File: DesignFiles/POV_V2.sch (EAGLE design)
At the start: 34 parts, among them CN1 1X4-CLEANBIG, CN2 1X4-CLEANBIG, CN3 1X4-CLEANBIG, CN4 1X4-CLEANBIG, IC1 SN74HC595, J1 PINHD-1X10, J2 PINHD-1X10

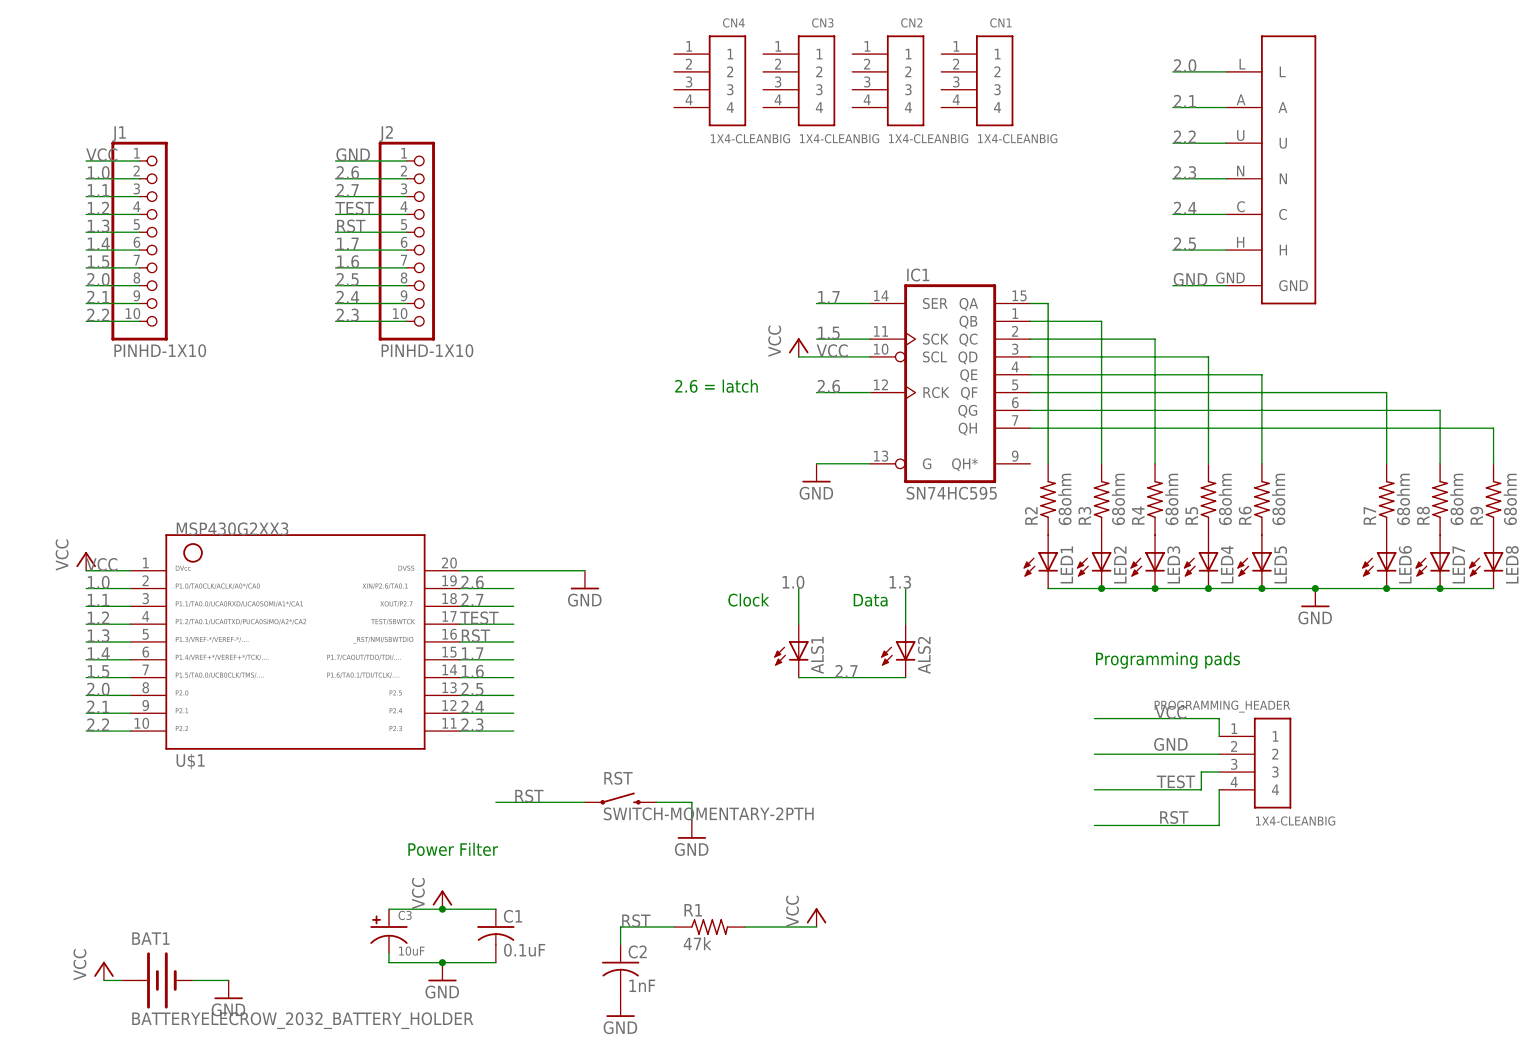
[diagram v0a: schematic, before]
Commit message: Had incorrect version of board uploaded
Correcting uploaded eagle board
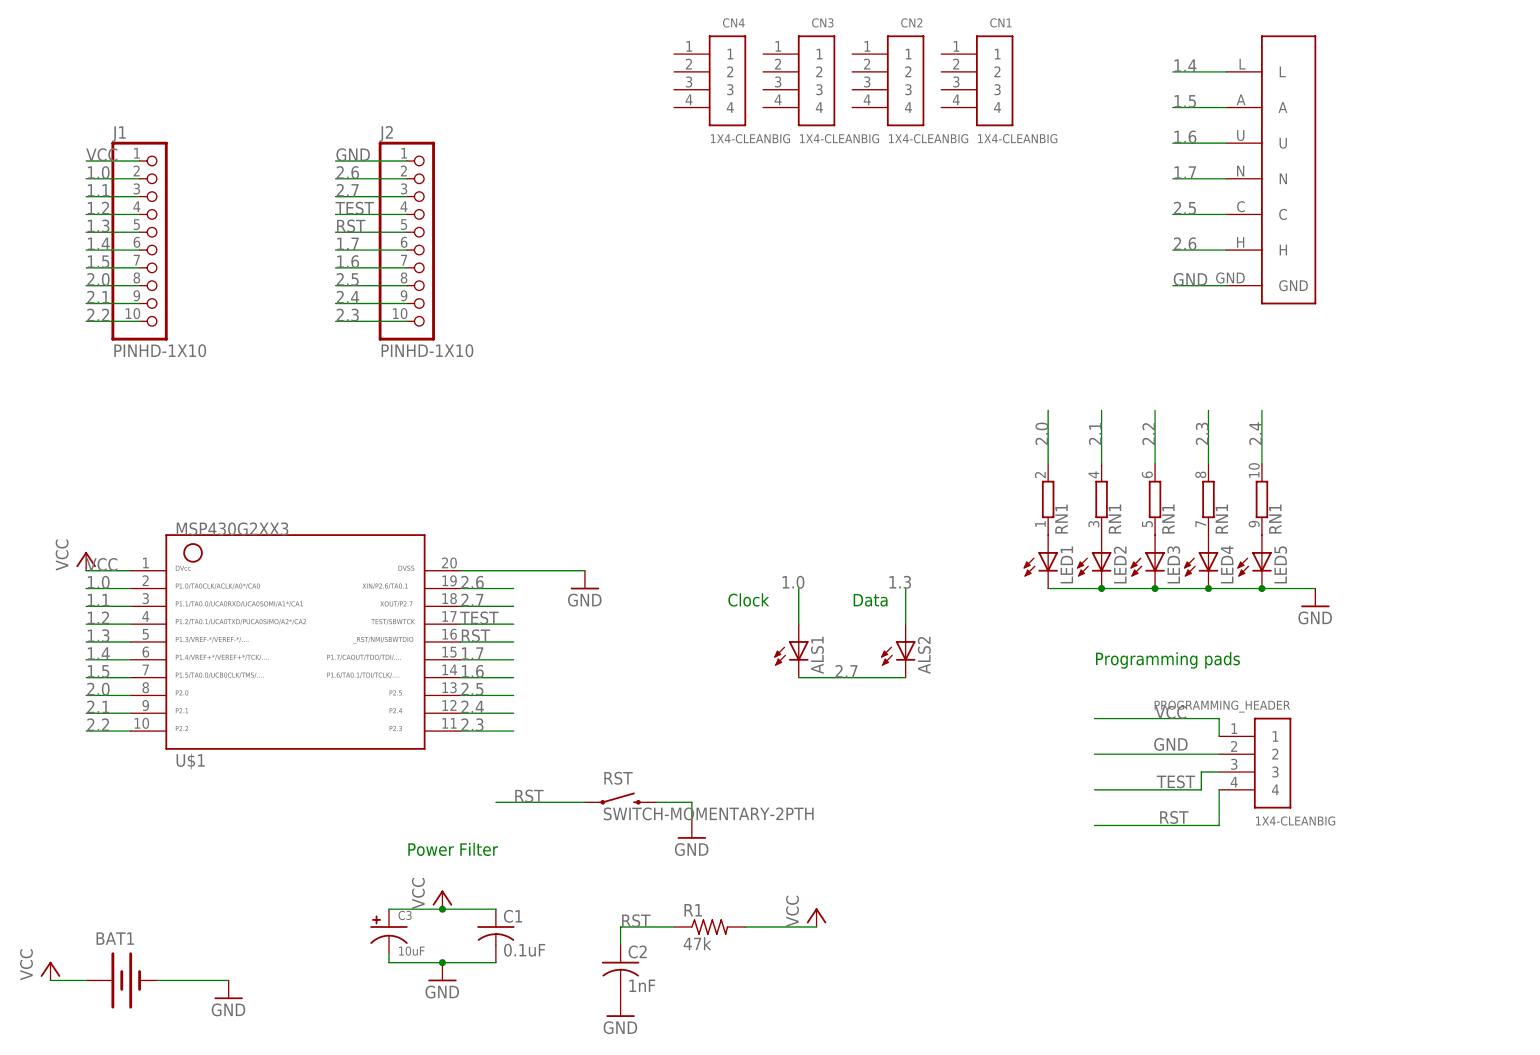
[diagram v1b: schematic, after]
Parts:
- removed IC1: SN74HC595, TIBadgeCustom:74LS595N
- removed LED6, LED7, LED8: (no value), led:LED3MM
- removed R2, R3, R4, R5, R6, R7, R8, R9: 68ohm, resistor:R-US_0204/7
- added RN1: (no value), resistor-sil:E5RP
- PROGRAMMING_HEADER: device BergCustom:1X4-CLEANBIG -> TIBadgeCustom:1X4-CLEANBIG
- R1: device rcl:R-US_0204/7 -> TIBadgeCustom:R-US_0204/7
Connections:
- removed net N$10: IC1A.QD, R5.2
- removed net N$11: IC1A.QE, R6.2
- removed net N$13: LED6.A, R7.1
- removed net N$14: LED7.A, R8.1
- removed net N$15: LED8.A, R9.1
- removed net N$16: IC1A.QF, R7.2
- removed net N$17: IC1A.QG, R8.2
- removed net N$18: IC1A.QH, R9.2
- removed net N$6: LED5.A, R6.1
- removed net N$7: IC1A.QA, R2.2
- removed net N$8: IC1A.QB, R3.2
- removed net N$9: IC1A.QC, R4.2
- new net N$1: LED1.A, RN1A.1
- net 1.4: now also U$5.L
- net 1.5: now also U$5.A; no longer IC1A.SCK
- net 1.6: now also U$5.U
- net 1.7: now also U$5.N; no longer IC1A.SER
- net 2.0: now also RN1A.2; no longer U$5.L
- net 2.1: now also RN1B.2; no longer U$5.A
- net 2.2: now also RN1C.2; no longer U$5.U
- net 2.3: now also RN1D.2; no longer U$5.N
- net 2.4: now also RN1E.2; no longer U$5.C
- net 2.5: now also U$5.C; no longer U$5.H
- net 2.6: now also U$5.H; no longer IC1A.RCK
- net GND: no longer IC1A.G, LED6.C, LED7.C, LED8.C
- net N$2: now also LED2.A, RN1B.1; no longer LED1.A, R2.1
- net N$3: now also LED3.A, RN1C.1; no longer LED2.A, R3.1
- net N$4: now also LED4.A, RN1D.1; no longer LED3.A, R4.1
- net N$5: now also LED5.A, RN1E.1; no longer LED4.A, R5.1
- net VCC: no longer IC1A.SCL
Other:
- note removed: "2.6 = latch"
- moved on the sheet: BAT1
